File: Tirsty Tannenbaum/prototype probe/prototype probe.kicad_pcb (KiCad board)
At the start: 2 copper layers, 66.7 x 162.6 mm, 9 parts, among them J1 Conn_01x06_Female, J2 Conn_01x03_Male

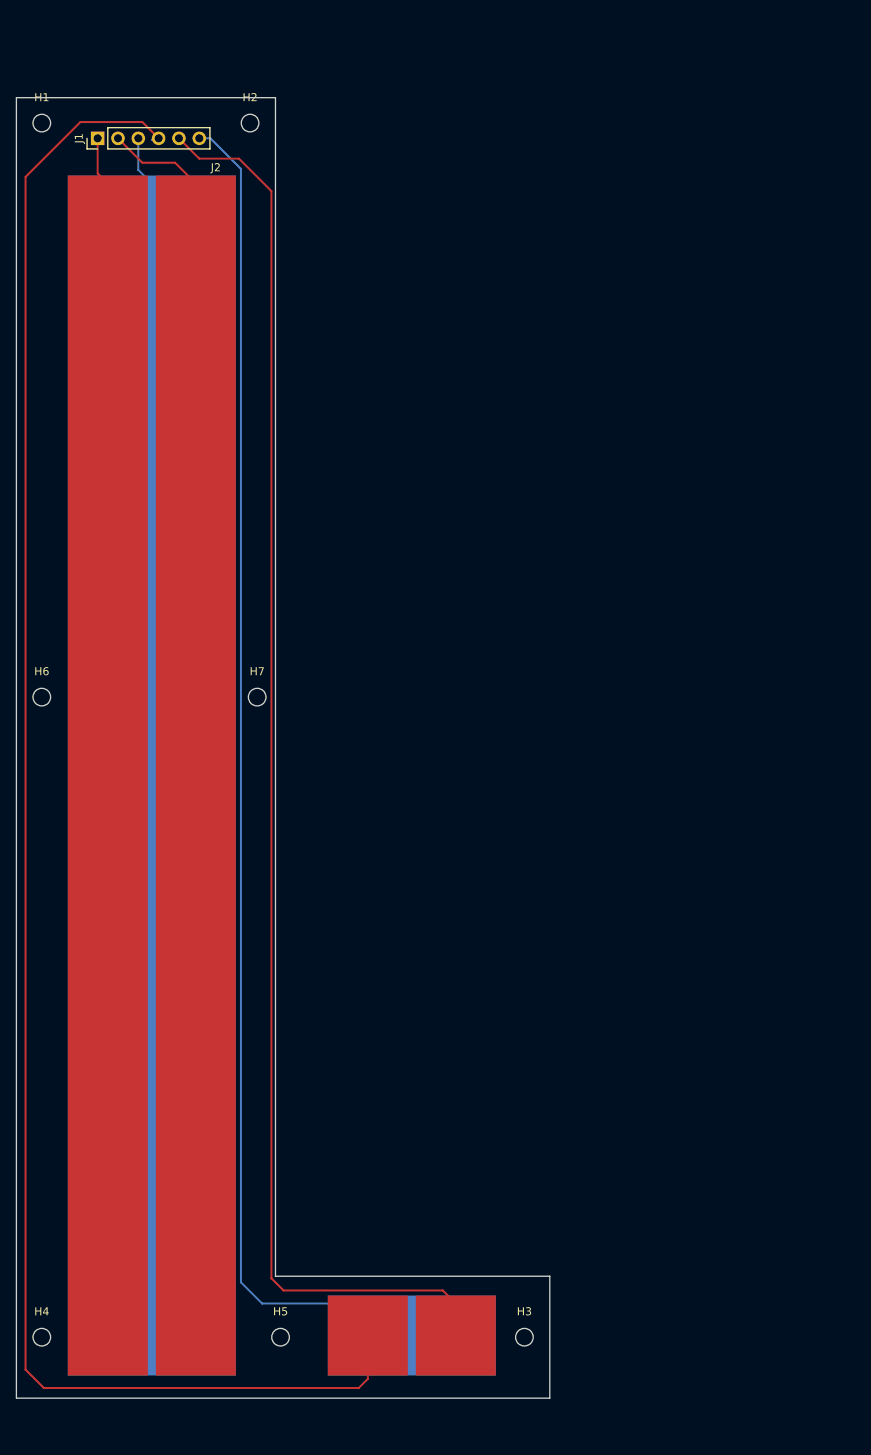
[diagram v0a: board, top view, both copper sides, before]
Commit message: Made dielectric comp section inline to save PCB costs, added option for inline ref caps
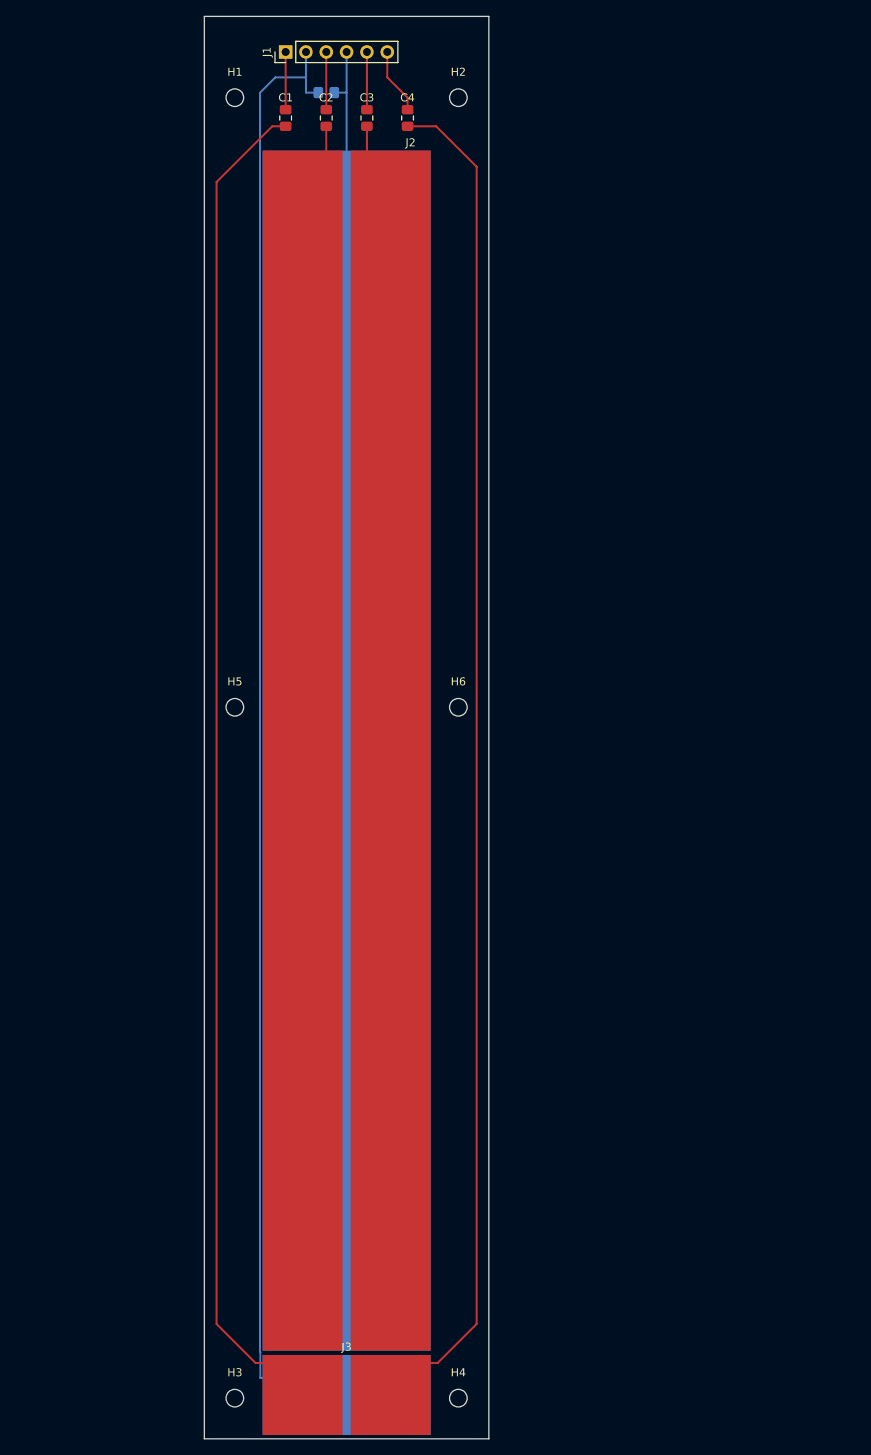
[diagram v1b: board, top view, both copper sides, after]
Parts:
- removed H7: MountingHole, MountingHole:MountingHole_2.2mm_M2
- added C1: C, Capacitor_SMD:C_0805_2012Metric_Pad1.18x1.45mm_HandSolder, F.Cu at (78.7, 27.9)
- added C2: C, Capacitor_SMD:C_0805_2012Metric_Pad1.18x1.45mm_HandSolder, F.Cu at (83.8, 27.9)
- added C3: C, Capacitor_SMD:C_0805_2012Metric_Pad1.18x1.45mm_HandSolder, F.Cu at (88.9, 27.9)
- added C4: C, Capacitor_SMD:C_0805_2012Metric_Pad1.18x1.45mm_HandSolder, F.Cu at (94.0, 27.9)
- added J3: Conn_01x03_Male, prototype probe:Cap-Electrode-Dielectric-Comp, F.Cu at (86.4, 182.6)
- added R1: R, Resistor_SMD:R_0805_2012Metric_Pad1.20x1.40mm_HandSolder, B.Cu at (83.8, 24.8)
- J1: value Conn_01x06_Female -> Conn_01x06_Male
- moved H5 78.9 mm to (72.4, 101.6)
- moved H4 52.6 mm to (100.3, 188.0)
- moved H6 52.1 mm to (100.3, 101.6)
- moved H3 37.0 mm to (72.4, 188.0)
- moved H2 26.2 mm to (100.3, 25.4)
- moved J1 25.9 mm to (78.7, 19.7)
- moved J2 24.5 mm to (86.4, 32.0)
- moved H1 24.3 mm to (72.4, 25.4)
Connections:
- J1 pad 1: Net-(J1-Pad1) -> Net-(C1-Pad2)
- J1 pad 3: Net-(J1-Pad3) -> Net-(C2-Pad2)
- J1 pad 5: Net-(J1-Pad5) -> Net-(C3-Pad2)
- J1 pad 6: Net-(J1-Pad6) -> Net-(C4-Pad2)
- J2 pad 1: Net-(J1-Pad1) -> Net-(C2-Pad1)
- J2 pad 2: Net-(J1-Pad2) -> Net-(C3-Pad1)
- J2 pad 3: Net-(J1-Pad3) -> Net-(J1-Pad4)
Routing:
- net Net-(J1-Pad4): track 223.3 -> 14.9 mm
- net Net-(J1-Pad5): track 174.5 -> 0.00 mm
- net Net-(J1-Pad2): track 12.1 -> 186.5 mm
- net Net-(C1-Pad1): track 0.00 -> 172.0 mm
- net Net-(J1-Pad6): track 168.4 -> 0.00 mm
- net Net-(C4-Pad1): track 0.00 -> 168.2 mm
- net Net-(C3-Pad1): track 0.00 -> 8.69 mm
- net Net-(C4-Pad2): track 0.00 -> 8.27 mm
- net Net-(C3-Pad2): track 0.00 -> 7.22 mm
- net Net-(C2-Pad2): track 0.00 -> 7.22 mm
- net Net-(C1-Pad2): track 0.00 -> 7.22 mm
- net Net-(C2-Pad1): track 0.00 -> 7.00 mm
- net Net-(J1-Pad3): track 6.36 -> 0.00 mm
- net Net-(J1-Pad1): track 6.18 -> 0.00 mm
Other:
- board size 66.7 x 162.6 mm -> 35.6 x 177.8 mm

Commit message: Silkscreen ruler in progress
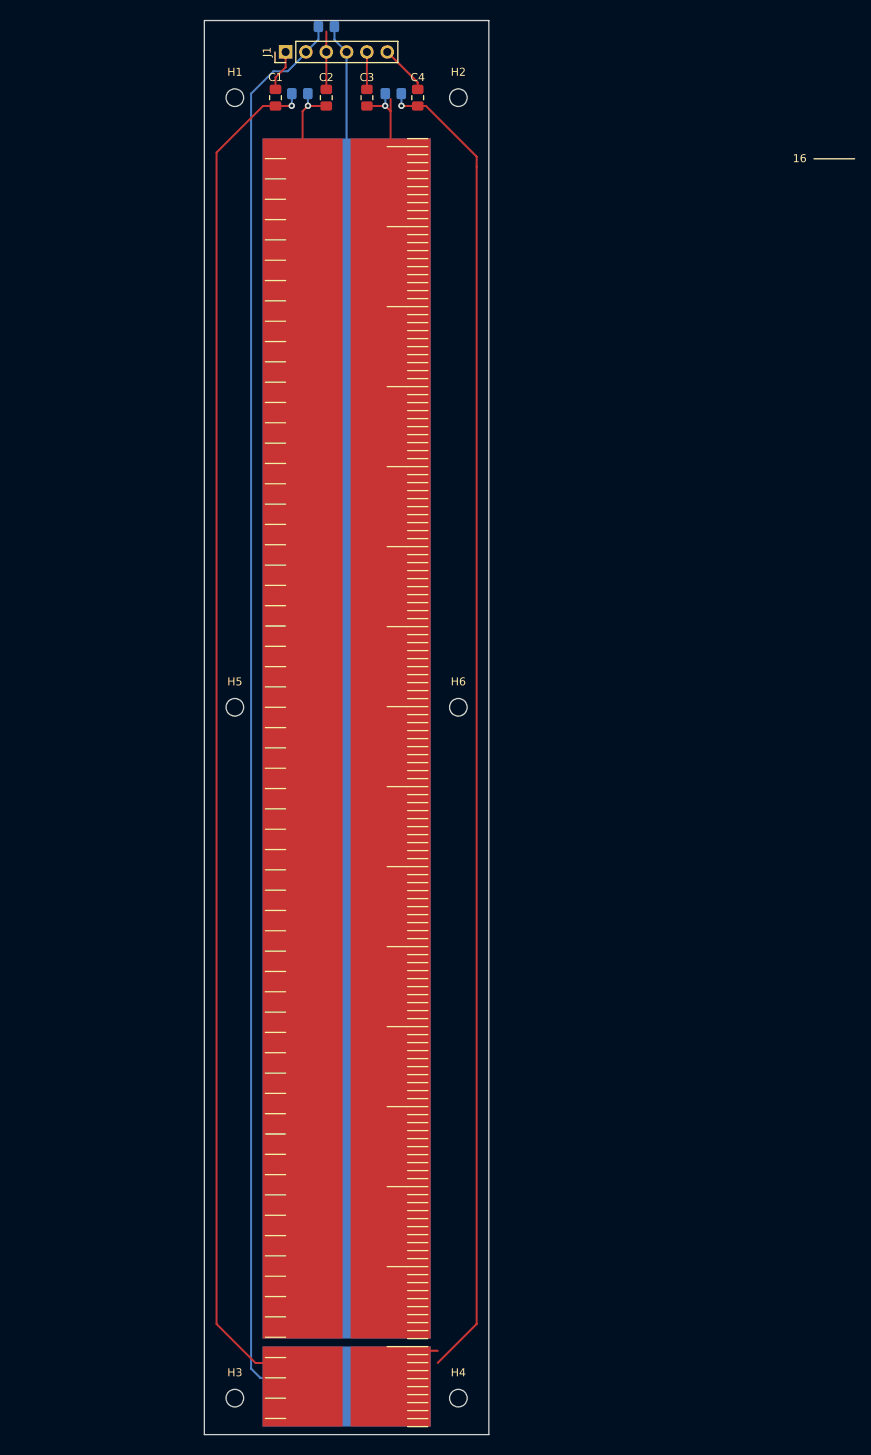
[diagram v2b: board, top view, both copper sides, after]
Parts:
- added R2: R, Resistor_SMD:R_0805_2012Metric_Pad1.20x1.40mm_HandSolder, B.Cu at (80.5, 24.9)
- added R3: R, Resistor_SMD:R_0805_2012Metric_Pad1.20x1.40mm_HandSolder, B.Cu at (92.2, 24.9)
- moved R1 8.26 mm to (83.8, 16.5)
- moved C1 2.84 mm to (77.5, 25.4)
- moved C4 2.84 mm to (95.2, 25.4)
- moved C2 2.54 mm to (83.8, 25.4)
- moved C3 2.54 mm to (88.9, 25.4)
- moved J2 1.52 mm to (86.4, 30.5)
- moved J3 1.06 mm to (86.4, 181.5)
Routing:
- net Net-(C3-Pad1): track 8.69 -> 15.4 mm, vias 0 -> 1
- net Net-(C1-Pad1): track 172.0 -> 177.0 mm, vias 0 -> 1
- net Net-(C4-Pad1): track 168.2 -> 172.5 mm, vias 0 -> 1
- net Net-(C2-Pad1): track 7.00 -> 10.2 mm, vias 0 -> 1
- net Net-(C3-Pad2): track 7.22 -> 4.68 mm
- net Net-(J1-Pad4): track 14.9 -> 17.1 mm
- net Net-(C4-Pad2): track 8.27 -> 6.26 mm
- net Net-(C1-Pad2): track 7.22 -> 5.20 mm
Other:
- board size 35.6 x 177.8 mm -> 35.6 x 176.8 mm
- board text added: "1"
- board text added: "10"
- board text added: "11"
- board text added: "12"
- board text added: "13"
- board text added: "14"
- board text added: "15"
- board text added: "16"
- board text added: "2"
- board text added: "3"
- board text added: "4"
- board text added: "5"
- board text added: "6"
- board text added: "7"
- board text added: "8"
- board text added: "9"

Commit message: Finished ruler
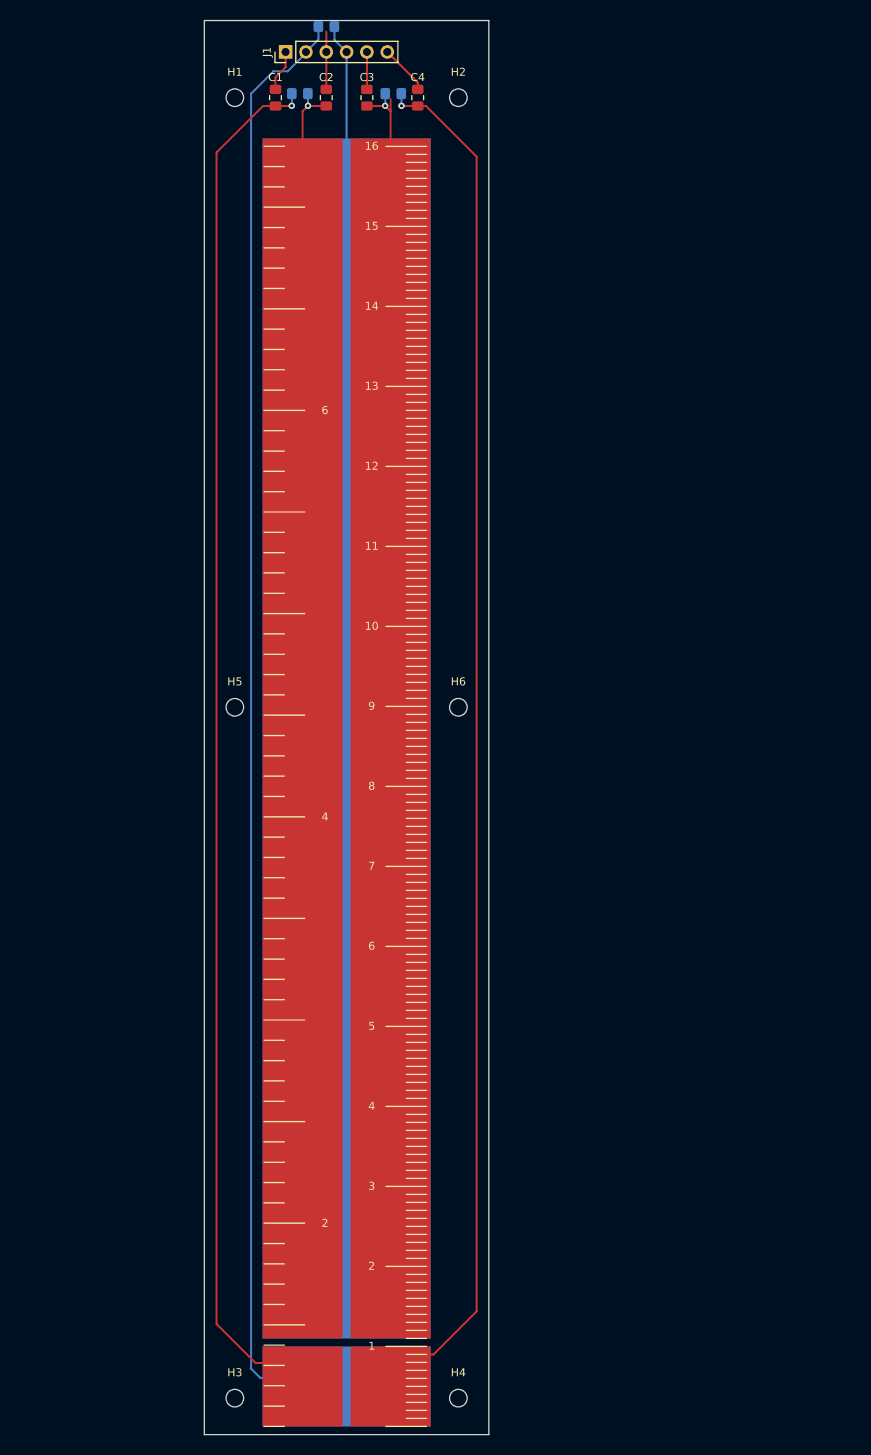
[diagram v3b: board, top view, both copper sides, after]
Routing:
- net Net-(C4-Pad1): track 172.5 -> 171.1 mm

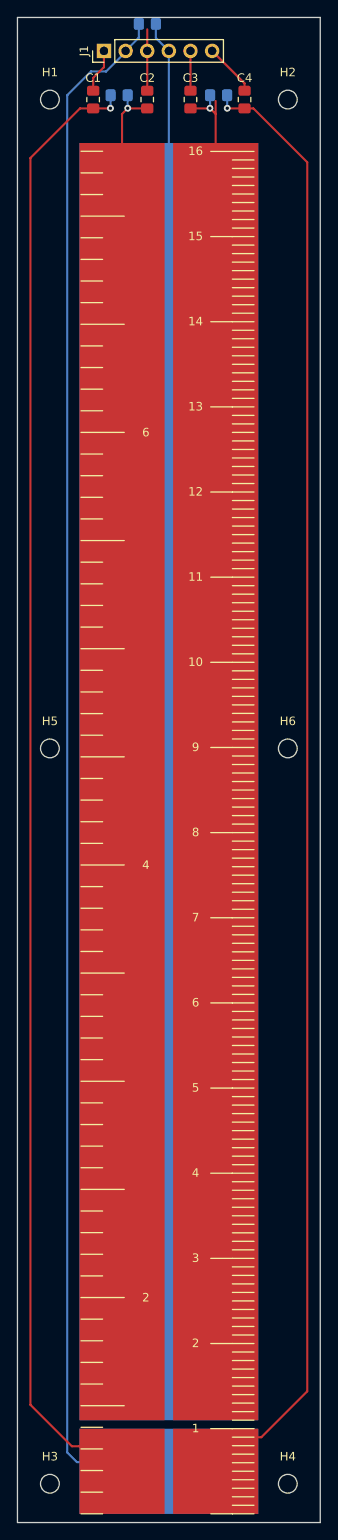
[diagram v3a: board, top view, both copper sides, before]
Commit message: Add ruler to bottom side
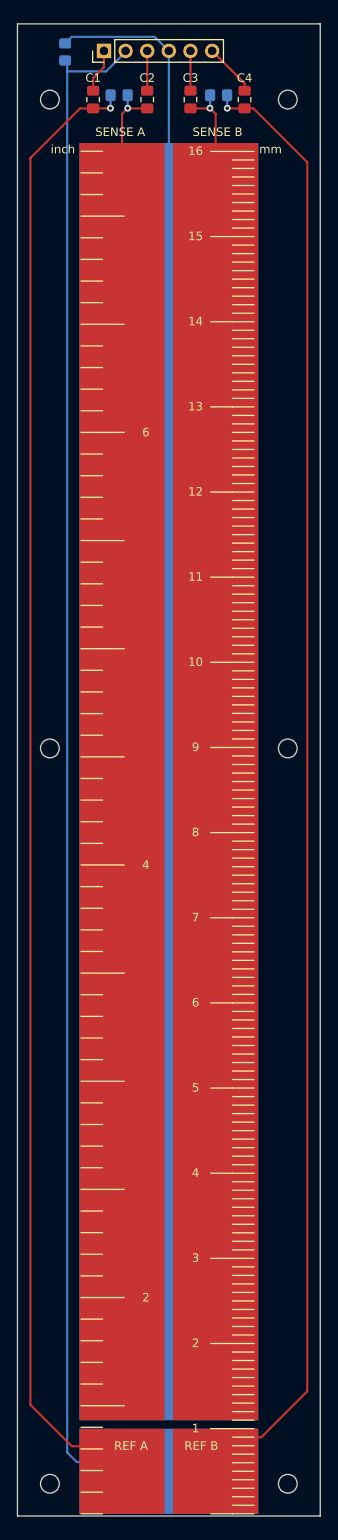
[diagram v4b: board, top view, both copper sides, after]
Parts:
- moved R1 10.2 mm to (74.2, 19.8), turned to 90 degrees
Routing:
- net Net-(J1-Pad4): track 17.1 -> 26.5 mm
- net Net-(C2-Pad2): track 7.22 -> 4.68 mm
- net Net-(C3-Pad1): track 15.4 -> 13.8 mm
- net Net-(J1-Pad2): track 186.6 -> 185.8 mm
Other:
- board size 35.6 x 176.8 mm -> 35.6 x 175.2 mm
- board text added: "RA"
- board text added: "RB"
- board text added: "REF A"
- board text added: "REF B"
- board text added: "RS"
- board text added: "SA"
- board text added: "SB"
- board text added: "SENSE A"
- board text added: "SENSE B"
- board text added: "SS"
- board text added: "Tirsty Tannenbaum Level Probe V1 11/19/2021"
- board text added: "inch"
- board text added: "mm"

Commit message: Add logo
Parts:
- added G***: LOGO, prototype probe:Tirsty Tannenbaum Logo 7200 DPI, B.Cu at (100.3, 158.8)
- added G***: LOGO, prototype probe:Tirsty Tannenbaum Logo 7200 DPI, B.Cu at (100.3, 118.1)
- added G***: LOGO, prototype probe:Tirsty Tannenbaum Logo 25mm_16mm, F.Cu at (100.3, 39.9)
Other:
- board text added: "Tirsty Tannenbaum Level Probe V1.0, Nov. 2021 www.spuriousemissions.com"
- board text removed: "Tirsty Tannenbaum Level Probe V1 11/19/2021"

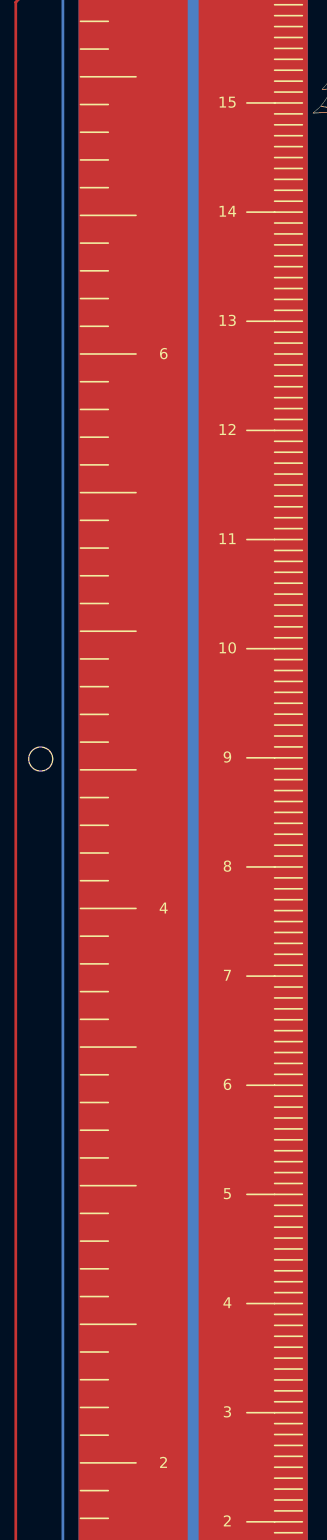
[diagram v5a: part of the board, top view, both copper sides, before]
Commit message: Convert to KiCad 6
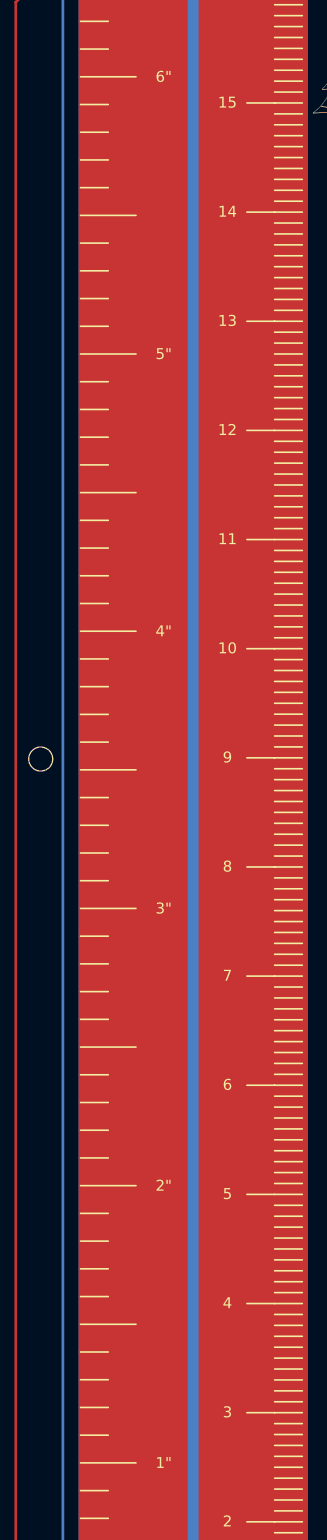
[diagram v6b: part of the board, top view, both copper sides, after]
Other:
- net class Default removed
- board text added: "1""
- board text added: "2""
- board text added: "3""
- board text added: "4""
- board text added: "5""
- board text added: "6""
